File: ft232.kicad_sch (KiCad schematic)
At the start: 20 parts, among them J3 tp_ft232_, Q1 2N7002, U3 FT232BM

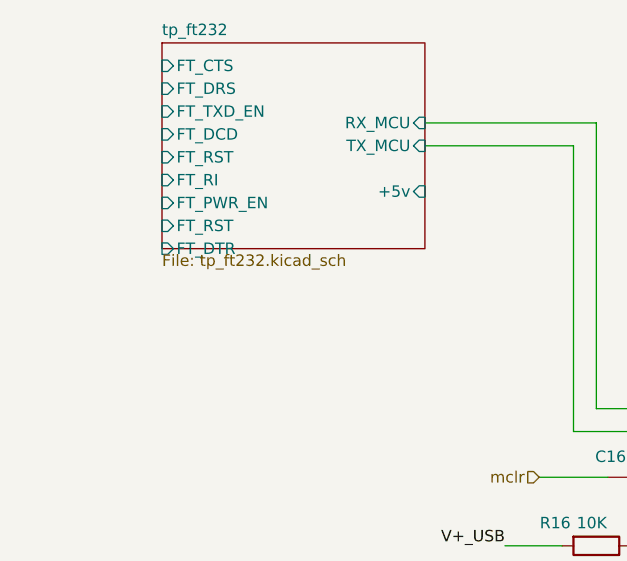
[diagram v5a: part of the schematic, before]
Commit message: feat: PCB layout updates, schematic changes, remove freerouting.dsn
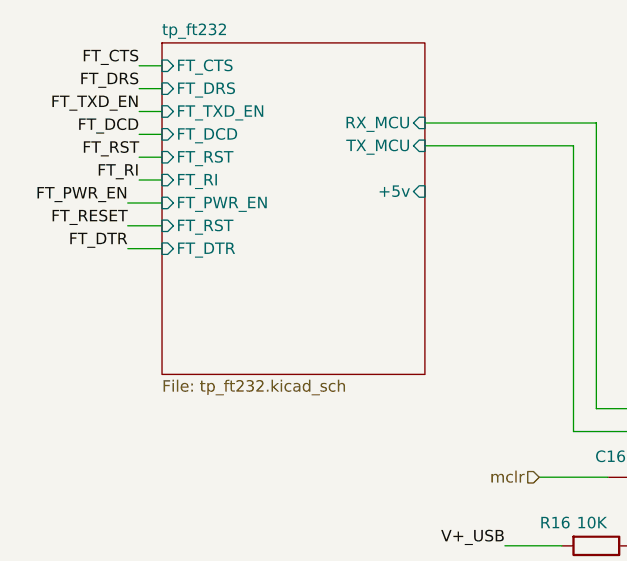
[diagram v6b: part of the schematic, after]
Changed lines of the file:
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@@
 	(wire
 		(pts
+			(xy 26.67 58.42) (xy 30.48 58.42)
+		)
+		(stroke
+			(width 0)
+			(type default)
+		)
+	)
+	(wire
+		(pts
 			(xy 113.03 129.54) (xy 113.03 130.81)
 		)
@@
 	(wire
 		(pts
+			(xy 27.94 43.18) (xy 30.48 43.18)
+		)
+		(stroke
+			(width 0)
+			(type default)
+		)
+	)
+	(wire
+		(pts
 			(xy 194.31 66.04) (xy 194.31 68.58)
 		)
@@
 	(wire
 		(pts
+			(xy 26.67 55.88) (xy 30.48 55.88)
+		)
+		(stroke
+			(width 0)
+			(type default)
+		)
+	)
+	(wire
+		(pts
 			(xy 173.99 124.46) (xy 170.18 124.46)
 		)
@@
 	(wire
 		(pts
+			(xy 27.94 50.8) (xy 30.48 50.8)
+		)
+		(stroke
+			(width 0)
+			(type default)
+		)
+	)
+	(wire
+		(pts
 			(xy 68.58 93.98) (xy 74.93 93.98)
 		)
@@
 	(wire
 		(pts
+			(xy 27.94 45.72) (xy 30.48 45.72)
+		)
+		(stroke
+			(width 0)
+			(type default)
+		)
+	)
+	(wire
+		(pts
 			(xy 97.79 129.54) (xy 97.79 124.46)
 		)
@@
 	(wire
 		(pts
+			(xy 26.67 60.96) (xy 30.48 60.96)
+		)
+		(stroke
+			(width 0)
+			(type default)
+		)
+	)
+	(wire
+		(pts
 			(xy 80.01 86.36) (xy 72.39 86.36)
 		)
@@
 	(wire
 		(pts
+			(xy 27.94 48.26) (xy 30.48 48.26)
+		)
+		(stroke
+			(width 0)
+			(type default)
+		)
+	)
+	(wire
+		(pts
+			(xy 27.94 53.34) (xy 30.48 53.34)
+		)
+		(stroke
+			(width 0)
+			(type default)
+		)
+	)
+	(wire
+		(pts
 			(xy 173.99 121.92) (xy 170.18 121.92)
 		)
@@
 	(wire
 		(pts
+			(xy 27.94 40.64) (xy 30.48 40.64)
+		)
+		(stroke
+			(width 0)
+			(type default)
+		)
+	)
+	(wire
+		(pts
 			(xy 109.22 146.05) (xy 109.22 140.97)
 		)
@@
 		)
 	)
+	(label "FT_TXD_EN"
+		(at 27.94 45.72 180)
+		(effects
+			(font
+				(size 1.27 1.27)
+			)
+			(justify right bottom)
+		)
+	)
 	(label "FT_RST"
 		(at 124.46 83.82 180)
@@
 		)
 	)
+	(label "FT_RESET"
+		(at 26.67 58.42 180)
+		(effects
+			(font
+				(size 1.27 1.27)
+			)
+			(justify right bottom)
+		)
+	)
 	(label "V+_USB"
 		(at 210.82 101.6 0)
@@
 		)
 	)
+	(label "FT_RI"
+		(at 27.94 53.34 180)
+		(effects
+			(font
+				(size 1.27 1.27)
+			)
+			(justify right bottom)
+		)
+	)
+	(label "FT_DCD"
+		(at 27.94 48.26 180)
+		(effects
+			(font
+				(size 1.27 1.27)
+			)
+			(justify right bottom)
+		)
+	)
 	(label "FT_PWR_EN"
 		(at 124.46 104.14 180)
@@
 		)
 	)
+	(label "FT_CTS"
+		(at 27.94 40.64 180)
+		(effects
+			(font
+				(size 1.27 1.27)
+			)
+			(justify right bottom)
+		)
+	)
 	(label "FT_DRS"
 		(at 124.46 91.44 180)
@@
 		)
 	)
+	(label "FT_DRS"
+		(at 27.94 43.18 180)
+		(effects
+			(font
+				(size 1.27 1.27)
+			)
+			(justify right bottom)
+		)
+	)
+	(label "FT_PWR_EN"
+		(at 26.67 55.88 180)
+		(effects
+			(font
+				(size 1.27 1.27)
+			)
+			(justify right bottom)
+		)
+	)
 	(label "FT_XTOUT"
 		(at 176.53 114.3 0)
@@
 		)
 	)
+	(label "FT_DTR"
+		(at 26.67 60.96 180)
+		(effects
+			(font
+				(size 1.27 1.27)
+			)
+			(justify right bottom)
+		)
+	)
 	(label "FT_TXD_EN"
 		(at 124.46 101.6 180)
@@
 		)
 	)
+	(label "FT_RST"
+		(at 27.94 50.8 180)
+		(effects
+			(font
+				(size 1.27 1.27)
+			)
+			(justify right bottom)
+		)
+	)
 	(hierarchical_label "mclr"
 		(shape input)
@@
 	(sheet
 		(at 30.48 38.1)
-		(size 29.21 22.86)
+		(size 29.21 36.83)
 		(exclude_from_sim no)
 		(in_bom yes)
@@
 		)
 		(property "Sheetfile" "tp_ft232.kicad_sch"
-			(at 30.48 61.5446 0)
+			(at 30.48 75.5146 0)
 			(show_name no)
 			(do_not_autoplace no)

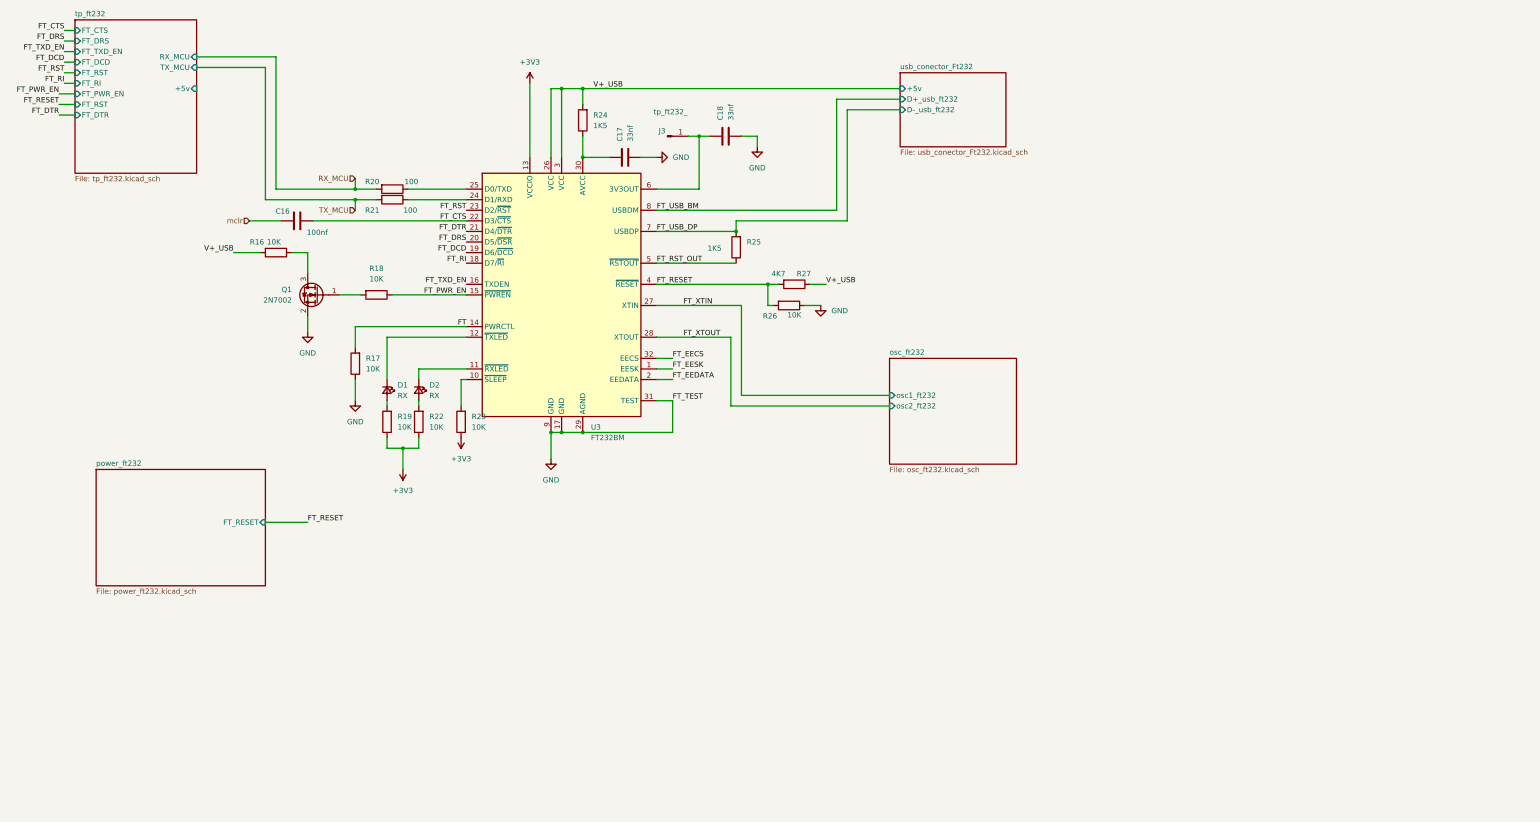
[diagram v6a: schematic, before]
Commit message: feat: 2-layer stackup, bus net class and schematic cleanup
PCB / project
- Reduce board from 4 layers to 2 (F.Cu / B.Cu) for cheaper fabrication
- Add "bus" net class and reorder net class priorities (bus 0, usb_differential 1, ...)

Schematics
- usb_conector_Ft232: add D+ / D-- labels on the USB mini-B data pair
- ft232: add 10K pull-ups, 100nf decoupling and test points on +3.3VA
- tp_ft232: remove solder jumpers JP1/JP2 (TX_Rpi / RX_Rpi now direct)
- Usb_pic32: add C38 100nf decoupling on +5V
- oled: expand connector J25 from 7 to 8 pins
- mcu / idc / power / zigbee / buttons / cnc_pic32: annotation and net cleanup

docs
- Add USB-Mini-B pinout reference images
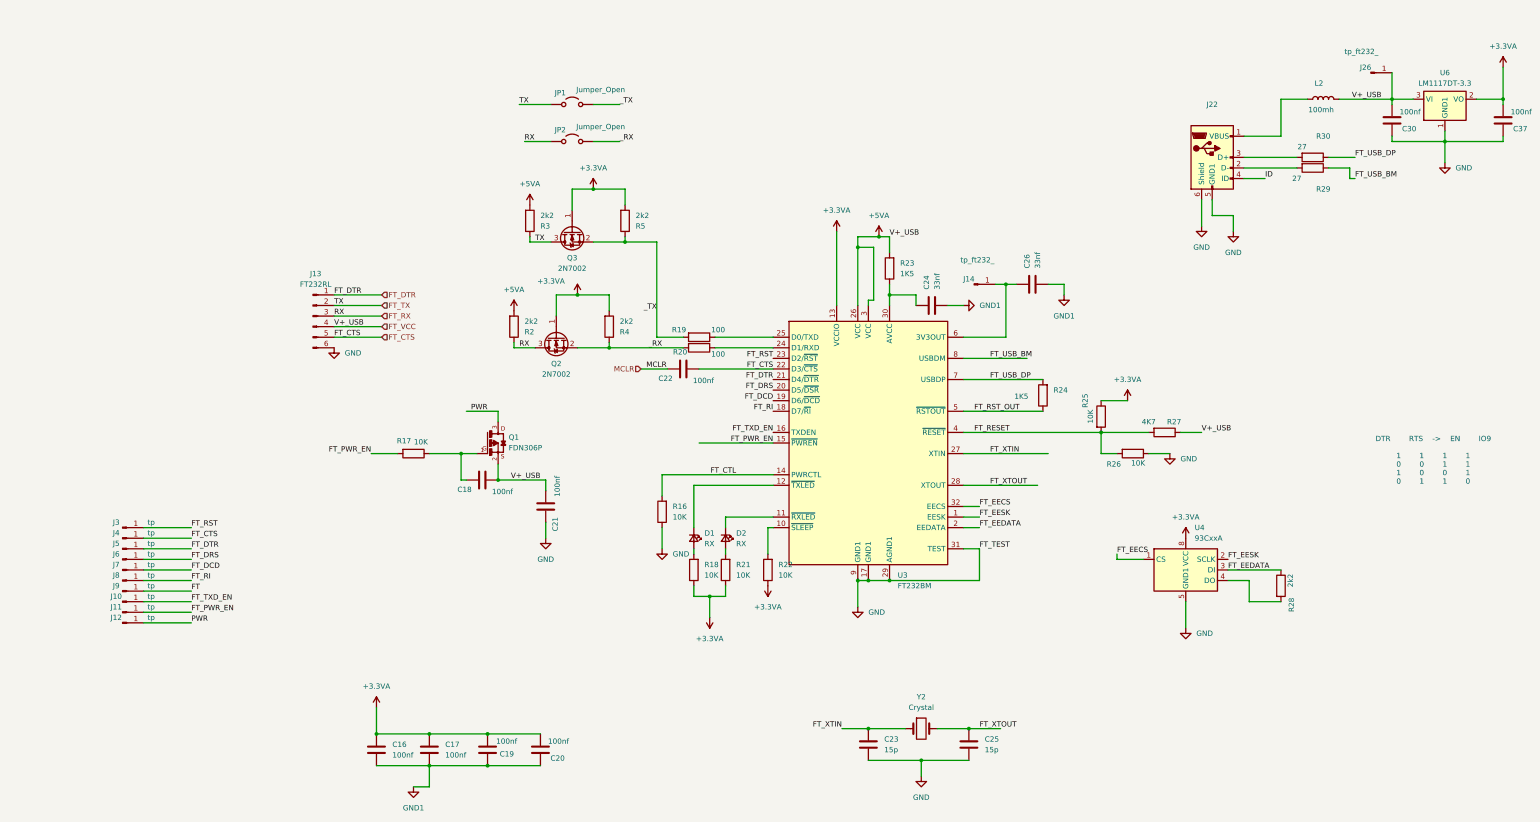
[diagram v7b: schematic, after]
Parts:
- removed Q1: 2N7002, Package_TO_SOT_SMD:SOT-23, symbol Transistor_FET:2N7002
- added C19, C20, C21, C22, C30, C37: 100nf, Capacitor_SMD:C_0805_2012Metric, symbol Device:C
- added C23, C25: 15p, Capacitor_SMD:C_0805_2012Metric, symbol Device:C
- added C24, C26: 33nf, Capacitor_SMD:C_0805_2012Metric, symbol Device:C
- added J10, J11, J4, J5, J6, J7, J8, J9: tp, TestPoint:TestPoint_Pad_D1.5mm, symbol Connector:Conn_01x01_Pin
- added J12: tp, TestPoint:TestPoint_THTPad_1.5x1.5mm_Drill0.7mm, symbol Connector:Conn_01x01_Pin
- added J13: FT232RL, Connector_PinHeader_2.54mm:PinHeader_1x06_P2.54mm_Vertical, symbol Connector:Conn_01x06_Pin
- added J14, J26: tp_ft232_, Library:connector_pin1, symbol Connector:Conn_01x01_Pin
- added J22: USB_B_Mini, kiC:USB_Mini-B_Lumberg_2486_01_Horizontal, symbol Connector:USB_B_Mini
- added JP1, JP2: Jumper_Open, Jumper:SolderJumper-2_P1.3mm_Open_RoundedPad1.0x1.5mm, symbol Jumper:Jumper_2_Open
- added L2: 100mh, Inductor_SMD:L_1206_3216Metric, symbol Device:L
- added Q1: FDN306P, Package_TO_SOT_SMD:SOT-23W, symbol FDN306P:FDN306P
- added Q2, Q3: 2N7002, Package_TO_SOT_SMD:SOT-23, symbol Transistor_FET:2N7002
- added R2, R28, R3, R4, R5: 2k2, Resistor_SMD:R_0805_2012Metric, symbol Device:R
- added R29, R30: 27, Resistor_SMD:R_0805_2012Metric, symbol Device:R
- added U4: 93CxxA, Package_SO:SOIC-8_5.3x5.3mm_P1.27mm, symbol Memory_EEPROM:93CxxA
- added U6: LM1117DT-3.3, kiC:SOT-223-3_TabPin2, symbol Regulator_Linear:LM1117DT-3.3
- added Y2: Crystal, Crystal:Resonator-2Pin_W10.0mm_H5.0mm, symbol Device:Crystal
- C17, C18: value 33nf -> 100nf
- J3: value tp_ft232_ -> tp; footprint Library:connector_pin1 -> TestPoint:TestPoint_Pad_D1.5mm
- R17: footprint Resistor_SMD:R_0805_2012Metric -> Resistor_SMD:R_0603_1608Metric
- R19: value 10K -> 100
- R21: value 100 -> 10K
- R23: value 10K -> 1K5
- R25: value 1K5 -> 10K
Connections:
- net TX_MCU is gone; now on an unnamed net: R21.2
- net mclr is gone; now on net +3.3VA: C16.1
- net FT: now also J9.1 (Pin_1); no longer R17.2, U3.14 (PWRCTL)
- net FT_CTS: now also C22.2, J13.5 (Pin_5), J4.1 (Pin_1); no longer C16.2
- net FT_DCD: now also J7.1 (Pin_1)
- net FT_DRS: now also J6.1 (Pin_1)
- net FT_DTR: now also J13.1 (Pin_1), J5.1 (Pin_1)
- net FT_EECS: now also U4.1 (CS)
- net FT_EEDATA: now also R28.1, U4.3 (DI)
- net FT_EESK: now also U4.2 (SCLK)
- net FT_PWR_EN: now also R17.2, J11.1 (Pin_1); no longer R18.1
- net FT_RESET: now also R25.2
- net FT_RI: now also J8.1 (Pin_1)
- net FT_RST: now also J3.1 (Pin_1)
- net FT_RST_OUT: now also R24.1; no longer R25.1
- net FT_TXD_EN: now also J10.1 (Pin_1)
- net FT_USB_BM: now also R30.1
- net FT_USB_DP: now also R24.2, R29.1; no longer R25.2
- net FT_XTIN: now also C23.1, Y2.1
- net FT_XTOUT: now also C25.1, Y2.2
- net GND: now also R16.1, C21.1, C23.2, C25.2, C30.1, C37.1, J13.6 (Pin_6), J22.5 (GND1), J22.6 (Shield), U4.5 (GND1), U6.1 (GND1); no longer C17.2, C18.2, R17.1
- net at U3.10 (~{SLEEP}): now also R22.2; no longer R23.2
- net at U3.24 (D1/RXD): now also R20.1; no longer R21.1
- net at U3.25 (D0/TXD): now also R19.1; no longer R20.1
- net at R18.2: now also D1.2 (A)
- net at D2.2 (A): no longer R22.2
- net _TX: now reaches R19.2
- net _TX: now also JP1.2 (B), Q3.2 (S), R5.1; no longer D1.2 (A)
- net +3V3 renamed +3.3VA
- net +3.3VA: now also C17.1, R18.1, R21.1, R25.1, C19.2, C20.2, C37.2, Q2.1 (G), Q3.1 (G), R4.2, R5.2, U4.8 (VCC), U6.2 (VO); no longer R19.1, R23.1
- net RX_MCU renamed _RX
- net _RX: now also JP2.2 (B), Q2.2 (S), R4.1
- net V+_USB renamed +5VA
- net +5VA: now also C18.2, R23.2, C21.2, C30.2, J13.4 (Pin_4), J26.1 (Pin_1), L2.2, Q1.2, R2.2, R3.2, U6.3 (VI); no longer R16.2, R24.2
- new net: J22.1 (VBUS), L2.1
- new net: C24.1, R23.1, U3.30 (AVCC)
- new net: C26.1, J14.1 (Pin_1), U3.6 (3V3OUT)
- new net: J22.3 (D+), R29.2
- new net: J22.2 (D-), R30.2
- new net: R28.2, U4.4 (DO)
- new net: C18.1, Q1.1, R17.1
- new net FT_CTL: R16.2, U3.14 (PWRCTL)
- new net FT_RX: J13.3 (Pin_3), JP2.1 (A), Q2.3 (D), R2.1
- new net FT_TX: J13.2 (Pin_2), JP1.1 (A), Q3.3 (D), R3.1
- new net GND1: C16.2, C17.2, C19.1, C20.1, C24.2, C26.2
- new net ID: J22.4 (ID)
- new net MCLR: C22.1
- new net PWR: J12.1 (Pin_1), Q1.3
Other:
- removed sheet osc_ft232
- removed sheet power_ft232
- removed sheet tp_ft232
- removed sheet usb_conector_Ft232
- note added: "DTR RTS -> EN IO9 1 1 1 1 0 0 1 1 1 0 0 1 0 1 1 0"

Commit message: add files
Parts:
- added JP24: Jumper_2_Bridged, symbol Jumper:Jumper_2_Bridged
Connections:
- net GND1 is gone; now on net GND: C16.2, C17.2, C19.1, C20.1, C24.2, C26.2
- net GND: now also JP24.2 (B); no longer J22.5 (GND1)
- net FT_USB_BM renamed FT_USB_DM
- new net: J22.5 (GND1), JP24.1 (A)
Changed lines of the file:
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@@
 	)
 	(junction
+		(at 232.41 104.14)
+		(diameter 0)
+		(color 0 0 0 0)
+	)
+	(junction
 		(at 129.54 209.55)
 		(diameter 0)
@@
 	(wire
 		(pts
+			(xy 232.41 96.52) (xy 232.41 104.14)
+		)
+		(stroke
+			(width 0)
+			(type default)
+		)
+	)
+	(wire
+		(pts
 			(xy 184.15 114.3) (xy 198.12 114.3)
 		)
@@
 	(wire
 		(pts
-			(xy 303.53 85.09) (xy 308.61 85.09)
-		)
-		(stroke
-			(width 0)
-			(type default)
-		)
-	)
-	(wire
-		(pts
 			(xy 359.41 72.39) (xy 359.41 67.31)
 		)
@@
 	(wire
 		(pts
-			(xy 308.61 85.09) (xy 308.61 88.9)
+			(xy 237.49 91.44) (xy 237.49 96.52)
 		)
 		(stroke
@@
 	(wire
 		(pts
+			(xy 237.49 96.52) (xy 232.41 96.52)
+		)
+		(stroke
+			(width 0)
+			(type default)
+		)
+	)
+	(wire
+		(pts
 			(xy 247.65 154.94) (xy 243.84 154.94)
 		)
@@
 	(wire
 		(pts
-			(xy 111.76 222.25) (xy 115.57 222.25)
-		)
-		(stroke
-			(width 0)
-			(type default)
-		)
-	)
-	(wire
-		(pts
 			(xy 226.06 90.17) (xy 226.06 93.98)
 		)
@@
 		)
 	)
-	(label "FT_USB_BM"
+	(label "FT_USB_DM"
 		(at 337.82 76.2 0)
 		(effects
@@
 		)
 	)
-	(label "FT_USB_BM"
+	(label "FT_USB_DM"
 		(at 250.19 119.38 0)
 		(effects
@@
 			)
 		)
-		(property "Value" "GND1"
-			(at 267.97 109.22 0)
+		(property "Value" "GND"
+			(at 270.51 105.4099 0)
 			(show_name no)
 			(do_not_autoplace no)
@@
 					(size 1.27 1.27)
 				)
+				(justify left)
 			)
 		)
@@
 			)
 		)
-		(property "Value" "GND1"
-			(at 247.65 106.68 90)
+		(property "Value" "GND"
+			(at 247.65 106.6799 90)
 			(show_name no)
 			(do_not_autoplace no)
@@
 	(symbol
 		(lib_id "power:GND1")
-		(at 308.61 88.9 0)
+		(at 313.69 85.09 0)
 		(unit 1)
 		(body_style 1)
@@
 		(fields_autoplaced yes)
 		(property "Reference" "#PWR084"
-			(at 308.61 95.25 0)
+			(at 313.69 91.44 0)
 			(hide yes)
 			(show_name no)
@@
 		)
 		(property "Value" "GND"
-			(at 308.61 93.98 0)
+			(at 313.69 90.17 0)
 			(show_name no)
 			(do_not_autoplace no)
@@
 		)
 		(property "Footprint" ""
-			(at 308.61 88.9 0)
+			(at 313.69 85.09 0)
 			(hide yes)
 			(show_name no)
@@
 		)
 		(property "Datasheet" ""
-			(at 308.61 88.9 0)
+			(at 313.69 85.09 0)
 			(hide yes)
 			(show_name no)
@@
 		)
 		(property "Description" ""
-			(at 308.61 88.9 0)
+			(at 313.69 85.09 0)
 			(show_name no)
 			(do_not_autoplace no)
@@
 	(symbol
 		(lib_id "power:GND1")
-		(at 111.76 222.25 0)
+		(at 115.57 222.25 0)
 		(unit 1)
 		(body_style 1)
@@
 		(fields_autoplaced yes)
 		(property "Reference" "#PWR022"
-			(at 111.76 228.6 0)
+			(at 115.57 228.6 0)
 			(hide yes)
 			(show_name no)
@@
 			)
 		)
-		(property "Value" "GND1"
-			(at 111.76 227.33 0)
+		(property "Value" "GND"
+			(at 118.11 223.5199 0)
 			(show_name no)
 			(do_not_autoplace no)
@@
 					(size 1.27 1.27)
 				)
+				(justify left)
 			)
 		)
 		(property "Footprint" ""
-			(at 111.76 222.25 0)
+			(at 115.57 222.25 0)
 			(hide yes)
 			(show_name no)
@@
 		)
 		(property "Datasheet" ""
-			(at 111.76 222.25 0)
+			(at 115.57 222.25 0)
 			(hide yes)
 			(show_name no)
@@
 		)
 		(property "Description" ""
-			(at 111.76 222.25 0)
+			(at 115.57 222.25 0)
 			(show_name no)
 			(do_not_autoplace no)
@@
 	)
 	(symbol
+		(lib_id "power:PWR_FLAG")
+		(at 237.49 91.44 0)
+		(unit 1)
+		(body_style 1)
+		(exclude_from_sim no)
+		(in_bom yes)
+		(on_board yes)
+		(in_pos_files yes)
+		(dnp no)
+		(fields_autoplaced yes)
+		(property "Reference" "#FLG03"
+			(at 237.49 89.535 0)
+			(hide yes)
+			(show_name no)
+			(do_not_autoplace no)
+			(effects
+				(font
+					(size 1.27 1.27)
+				)
+			)
+		)
+		(property "Value" "PWR_FLAG"
+			(at 237.49 86.36 0)
+			(show_name no)
+			(do_not_autoplace no)
+			(effects
+				(font
+					(size 1.27 1.27)
+				)
+			)
+		)
+		(property "Footprint" ""
+			(at 237.49 91.44 0)
+			(hide yes)
+			(show_name no)
+			(do_not_autoplace no)
+			(effects
+				(font
+					(size 1.27 1.27)
+				)
+			)
+		)
+		(property "Datasheet" ""
+			(at 237.49 91.44 0)
+			(hide yes)
+			(show_name no)
+			(do_not_autoplace no)
+			(effects
+				(font
+					(size 1.27 1.27)
+				)
+			)
+		)
+		(property "Description" "Special symbol for telling ERC where power comes from"
+			(at 237.49 91.44 0)
+			(hide yes)
+			(show_name no)
+			(do_not_autoplace no)
+			(effects
+				(font
+					(size 1.27 1.27)
+				)
+			)
+		)
+		(pin "1"
+		)
+		(instances
+			(project "cnc_pic32"
+				(path "/13dbfc1f-be47-44ca-9042-3d6a9a657d7d/22a12b0c-67ed-4f76-a580-7ac736b63dbd"
+					(reference "#FLG03")
+					(unit 1)
+				)
+			)
+		)
+	)
+	(symbol
 		(lib_id "power:GND1")
 		(at 300.99 87.63 0)
@@
 		(in_pos_files yes)
 		(dnp no)
-		(fields_autoplaced yes)
 		(property "Reference" "R23"
-			(at 228.6 96.52 0)
+			(at 227.838 94.234 0)
 			(show_name no)
 			(do_not_autoplace no)
@@
 		)
 		(property "Value" "1K5"
-			(at 228.6 99.06 0)
+			(at 228.092 97.79 0)
 			(show_name no)
 			(do_not_autoplace no)
@@
 	)
 	(symbol
+		(lib_id "Jumper:Jumper_2_Bridged")
+		(at 308.61 85.09 0)
+		(unit 1)
+		(body_style 1)
+		(exclude_from_sim no)
+		(in_bom yes)
+		(on_board yes)
+		(in_pos_files yes)
+		(dnp no)
+		(fields_autoplaced yes)
+		(property "Reference" "JP24"
+			(at 308.61 80.01 0)
+			(show_name no)
+			(do_not_autoplace no)
+			(effects
+				(font
+					(size 1.27 1.27)
+				)
+			)
+		)
+		(property "Value" "Jumper_2_Bridged"
+			(at 308.61 82.55 0)
+			(show_name no)
+			(do_not_autoplace no)
+			(effects
+				(font
+					(size 1.27 1.27)
+				)
+			)
+		)
+		(property "Footprint" ""
+			(at 308.61 85.09 0)
+			(hide yes)
+			(show_name no)
+			(do_not_autoplace no)
+			(effects
+				(font
+					(size 1.27 1.27)
+				)
+			)
+		)
+		(property "Datasheet" ""
+			(at 308.61 90.17 0)
+			(hide yes)
+			(show_name no)
+			(do_not_autoplace no)
+			(effects
+				(font
+					(size 1.27 1.27)
+				)
+			)
+		)
+		(property "Description" "Jumper, 2-pole, closed/bridged"
+			(at 308.61 92.71 0)
+			(hide yes)
+			(show_name no)
+			(do_not_autoplace no)
+			(effects
+				(font
+					(size 1.27 1.27)
+				)
+			)
+		)
+		(pin "1"
+		)
+		(pin "2"
+		)
+		(instances
+			(project "cnc_pic32"
+				(path "/13dbfc1f-be47-44ca-9042-3d6a9a657d7d/22a12b0c-67ed-4f76-a580-7ac736b63dbd"
+					(reference "JP24")
+					(unit 1)
+				)
+			)
+		)
+	)
+	(symbol
 		(lib_id "Device:Crystal")
 		(at 233.68 208.28 0)
@@
 			)
 		)
-		(property "Description" "Two pin crystal"
+		(property "Description" "Two pin crystal 6mhz"
 			(at 233.68 208.28 0)
 			(hide yes)
